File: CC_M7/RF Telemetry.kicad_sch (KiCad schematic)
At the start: 24 parts, among them U6 nRF52820-QDxx, U7 NRF21540-QDAA-R7, Y2 32MHz

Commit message: update
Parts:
- removed C43: 4.7uF, symbol Device:C_Small
- added J15: Conn_02x05_Odd_Even, symbol Connector_Generic:Conn_02x05_Odd_Even
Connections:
- net +3.3V: now also J15.10 (Pin_10)
- net GND: now also J15.2 (Pin_2), J15.6 (Pin_6), J15.8 (Pin_8)
- net RESET: now reaches U6.16 (P0.18/~{RESET})
- net RESET: now also J15.1 (Pin_1)
- net VBUS: no longer names the net of U6.10 (VBUS)
- new net SWCLCK: J15.7 (Pin_7)
- new net SWDIO: J15.9 (Pin_9)
- new net SWO: J15.5 (Pin_5)
- no-connect marks 0 -> 1
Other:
- note added: "Antenna"
- note added: "SWO Pins"
- note added: "VBUS hattı USB kullanılacağı zaman bağlanılacak."
- note added: "nRF OSC"
- note added: "nRF21540"
- note added: "nRF52820 and Decoupling"
- note removed: "VBUS hattı usb 5V hattı demektir"
- moved on the sheet: AE1, C31, C32, C33, C34, C35, C36, C37, C38, C39, C40, C41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

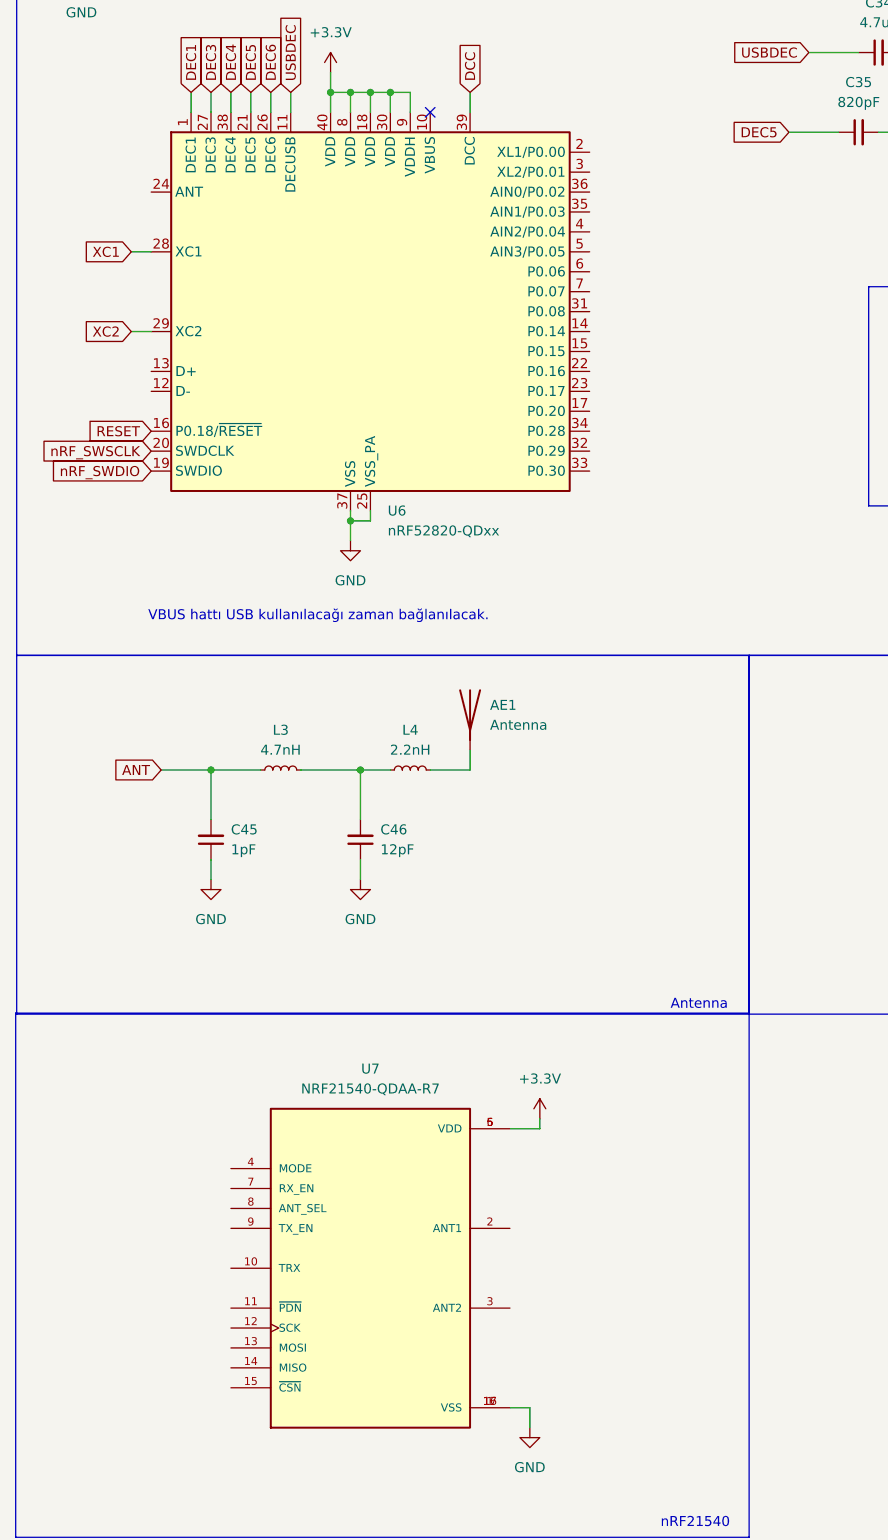
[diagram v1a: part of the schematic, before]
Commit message: NRF pins updated
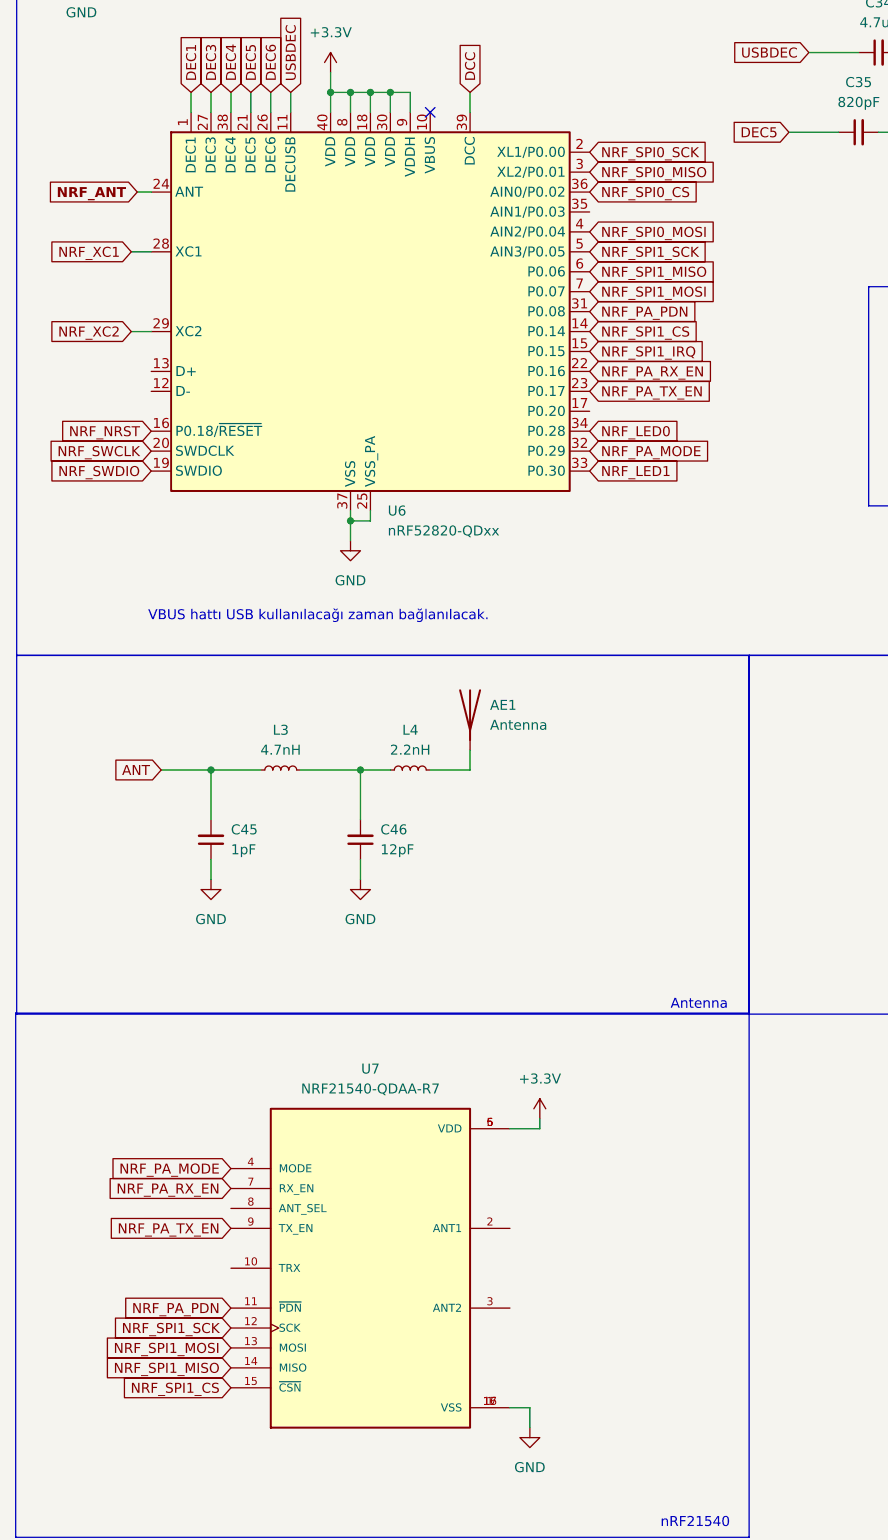
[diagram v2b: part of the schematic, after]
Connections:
- net RESET: no longer U6.16 (P0.18/~{RESET})
- net XC1: no longer U6.28 (XC1)
- net XC2: no longer U6.29 (XC2)
- net NRF_SPI1_CS: now reaches U6.14 (P0.14)
- net NRF_SPI1_CS: now also U7.15 (~{CSN})
- net NRF_SPI1_IRQ: now reaches U6.15 (P0.15)
- net NRF_SPI0_SCK: now reaches U6.2 (XL1/P0.00)
- net NRF_PA_RX_EN: now reaches U6.22 (P0.16)
- net NRF_PA_RX_EN: now also U7.7 (RX_EN)
- net NRF_PA_TX_EN: now reaches U6.23 (P0.17)
- net NRF_PA_TX_EN: now also U7.9 (TX_EN)
- net NRF_ANT: now reaches U6.24 (ANT)
- net NRF_SPI0_MISO: now reaches U6.3 (XL2/P0.01)
- net NRF_PA_PDN: now reaches U6.31 (P0.08)
- net NRF_PA_PDN: now also U7.11 (~{PDN})
- net NRF_PA_MODE : now reaches U6.32 (P0.29)
- net NRF_PA_MODE : now also U7.4 (MODE)
- net NRF_LED1: now reaches U6.33 (P0.30)
- net NRF_LED0: now reaches U6.34 (P0.28)
- net NRF_SPI0_CS: now reaches U6.36 (AIN0/P0.02)
- net NRF_SPI0_MOSI: now reaches U6.4 (AIN2/P0.04)
- net NRF_SPI1_SCK: now reaches U6.5 (AIN3/P0.05)
- net NRF_SPI1_SCK: now also U7.12 (SCK)
- net NRF_SPI1_MISO : now reaches U6.6 (P0.06)
- net NRF_SPI1_MISO : now also U7.14 (MISO)
- net NRF_SPI1_MOSI: now reaches U6.7 (P0.07)
- net NRF_SPI1_MOSI: now also U7.13 (MOSI)
- net nRF_SWDIO renamed NRF_SWDIO
- net nRF_SWSCLK renamed NRF_SWCLK
- new net NRF_NRST: U6.16 (P0.18/~{RESET})
- new net NRF_XC1: U6.28 (XC1)
- new net NRF_XC2: U6.29 (XC2)

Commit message: NRF
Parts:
- removed AE1: Antenna, symbol Device:Antenna
- removed C45: 1pF, symbol Device:C_Small
- removed C46: 12pF, symbol Device:C_Small
- removed L3: 4.7nH, symbol Device:L_Small
- removed L4: 2.2nH, symbol Device:L_Small
- added C28: 2pF, symbol Device:C_Small
- added C29: 1pF, symbol Device:C_Small
- added J9: Antenna, SMA_CONNECTOR:LPRS_SMA_CONNECTOR, symbol SMA_CONNECTOR:SMA_CONNECTOR
- added L6: 1.9nH, symbol Device:L_Small
- added L7: 3.0nH, symbol Device:L_Small
- added R15: 10k, symbol Device:R_Small
- added R16: 50R, symbol Device:R_Small
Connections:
- net GND: now also U7.8 (ANT_SEL), C28.2, C29.2, J9.G1, J9.G2, J9.G3, J9.G4, R16.2
- net NRF_ANT: now also U7.10 (TRX)
- net NRF_PA_MODE : now also R15.1; no longer U7.4 (MODE)
- net at U7.2 (ANT1): now also L6.1
- net at U7.3 (ANT2): now also R16.1
- new net: C28.1, L6.2, L7.1
- new net: C29.1, J9.1, L7.2
- new net: R15.2, U7.4 (MODE)
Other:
- note removed: "Antenna"
- note removed: "VBUS hattı USB kullanılacağı zaman bağlanılacak."
- moved on the sheet: C31, C32, C33, C34, C35, C36, C37, C44, J15, L1, L2, U7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

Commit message: nrf
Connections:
- net RESET is gone; now on net NRF_NRST: J15.1 (Pin_1)
- net SWCLCK is gone; now on net NRF_SWCLK: J15.7 (Pin_7)
- net SWDIO is gone; now on net NRF_SWDIO: J15.9 (Pin_9)
- net NRF_PA_MODE  renamed NRF_PA_MODE
- net NRF_SPI1_MISO  renamed NRF_SPI1_MISO
- net SWO: no longer names the net of J15.5 (Pin_5)
- no-connect marks 1 -> 4

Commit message: final schematic 6 warning
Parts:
- removed J15: Conn_02x05_Odd_Even, symbol Connector_Generic:Conn_02x05_Odd_Even
- added D5, D6: LED, symbol Device:LED
- added JP5, JP6, JP7, JP8: SWDIO, symbol Jumper:Jumper_2_Bridged
- added R17, R2: 1.5k, symbol Device:R_Small
- J9: value Antenna -> SMA_CONNECTOR
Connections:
- net XC1 is gone; now on net NRF_XC1: C32.2, Y2.1
- net XC2 is gone; now on net NRF_XC2: C44.2, Y2.3
- net GND: now also R17.1, R2.1
- net NRF_LED0: now also D5.2 (A)
- net NRF_LED1: now also D6.2 (A)
- net NRF_NRST: now also JP8.1 (A)
- net NRF_SPI0_CS: now also U7.15 (~{CSN})
- net NRF_SPI0_MISO: now also U7.14 (MISO)
- net NRF_SPI0_MOSI: now also U7.13 (MOSI)
- net NRF_SPI0_SCK: now also U7.12 (SCK)
- net NRF_SWCLK: now also JP6.1 (A)
- net NRF_SWDIO: now also JP7.1 (A)
- net +3.3V renamed 3V3_RF
- net 3V3_RF: now also JP5.1 (A)
- net NRF_SPI1_CS renamed SPI3_CS
- net SPI3_CS: no longer U7.15 (~{CSN})
- net NRF_SPI1_IRQ renamed SPI3_IRQ
- net NRF_SPI1_MISO renamed SPI3_MISO
- net SPI3_MISO: no longer U7.14 (MISO)
- net NRF_SPI1_MOSI renamed SPI3_MOSI
- net SPI3_MOSI: no longer U7.13 (MOSI)
- net NRF_SPI1_SCK renamed SPI3_SCK
- net SPI3_SCK: no longer U7.12 (SCK)
- new net: D6.1 (K), R17.2
- new net: D5.1 (K), R2.2
- new net J2_32: JP5.2 (B)
- new net J2_36: JP6.2 (B)
- new net J2_38: JP7.2 (B)
- new net J2_40: JP8.2 (B)
- no-connect marks 4 -> 5
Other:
- note added: "SWO"
- note added: "nRF52820"
- note removed: "SWO Pins"
- note removed: "nRF52820 and Decoupling"
- moved on the sheet: C28, C29, C31, C32, C33, C34, C35, C36, C37, C38, C39, C40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

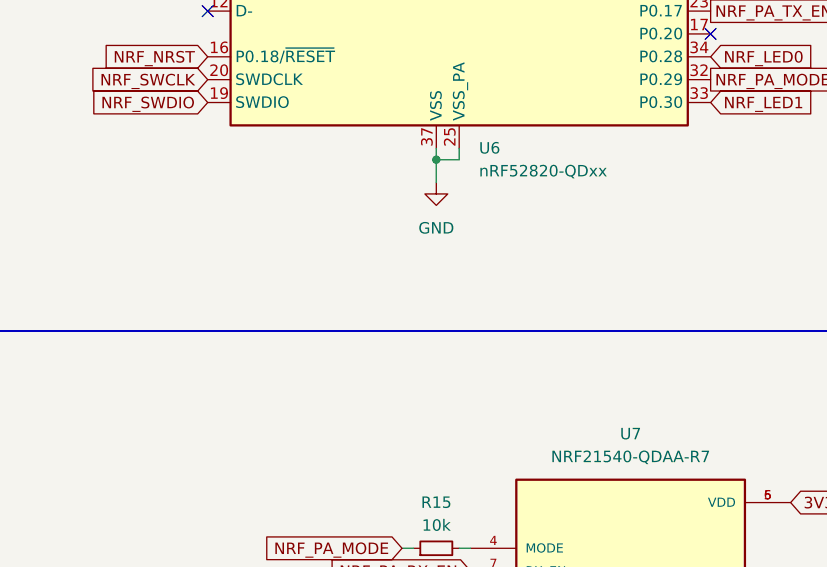
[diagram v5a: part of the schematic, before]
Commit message: schematic control comment
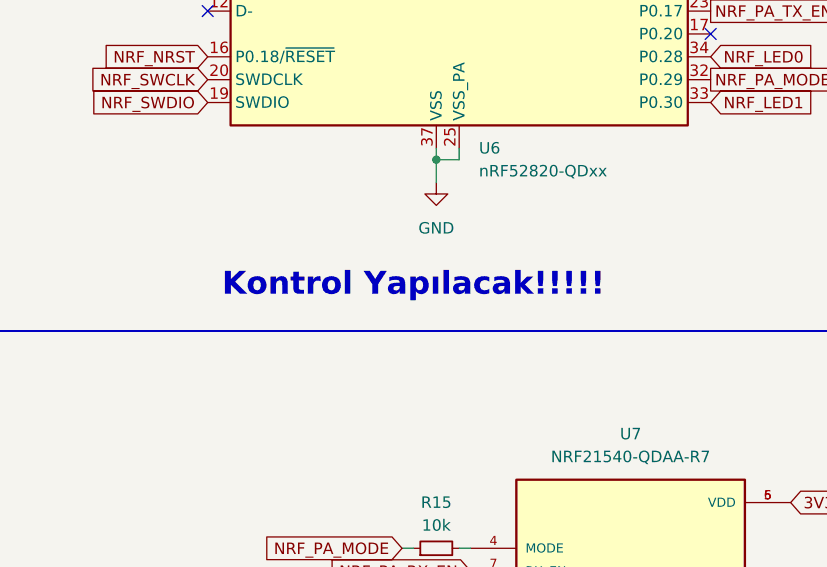
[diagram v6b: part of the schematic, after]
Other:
- note added: "Kontrol Yapılacak!!!!!"
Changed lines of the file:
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@@
+		)
+	)
+	(text "Kontrol Yapılacak!!!!!"
+		(exclude_from_sim no)
+		(at 69.85 139.7 0)
+		(effects
+			(font
+				(size 2.54 2.54)
+				(thickness 0.508)
+				(bold yes)
+			)
 		)
 	)

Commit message: Footprint assignment 1/2
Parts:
- C28, C29, C36, C39: footprint (none) -> Capacitor_SMD:C_0402_1005Metric
- C31, C32, C33, C35, C37, C38, C41, C42, C44: footprint (none) -> Capacitor_SMD:C_0201_0603Metric
- C34, C40: footprint (none) -> Capacitor_SMD:C_0603_1608Metric
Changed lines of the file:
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@@
 			)
 		)
-		(property "Footprint" ""
+		(property "Footprint" "Capacitor_SMD:C_0603_1608Metric"
 			(at 39.37 31.75 0)
 			(effects
@@
 			)
 		)
-		(property "Footprint" ""
+		(property "Footprint" "Capacitor_SMD:C_0201_0603Metric"
 			(at 69.85 31.75 0)
 			(effects
@@
 			)
 		)
-		(property "Footprint" ""
+		(property "Footprint" "Capacitor_SMD:C_0201_0603Metric"
 			(at 170.18 36.83 0)
 			(effects
@@
 			)
 		)
-		(property "Footprint" ""
+		(property "Footprint" "Capacitor_SMD:C_0402_1005Metric"
 			(at 170.18 26.67 0)
 			(effects
@@
 			)
 		)
-		(property "Footprint" ""
+		(property "Footprint" "Capacitor_SMD:C_0201_0603Metric"
 			(at 59.69 31.75 0)
 			(effects
@@
 			)
 		)
-		(property "Footprint" ""
+		(property "Footprint" "Capacitor_SMD:C_0402_1005Metric"
 			(at 30.48 31.75 0)
 			(effects
@@
 			)
 		)
-		(property "Footprint" ""
+		(property "Footprint" "Capacitor_SMD:C_0201_0603Metric"
 			(at 181.61 97.79 0)
 			(effects
@@
 			)
 		)
-		(property "Footprint" ""
+		(property "Footprint" "Capacitor_SMD:C_0402_1005Metric"
 			(at 142.24 181.61 0)
 			(effects
@@
 			)
 		)
-		(property "Footprint" ""
+		(property "Footprint" "Capacitor_SMD:C_0603_1608Metric"
 			(at 97.79 26.67 0)
 			(effects
@@
 			)
 		)
-		(property "Footprint" ""
+		(property "Footprint" "Capacitor_SMD:C_0201_0603Metric"
 			(at 49.53 31.75 0)
 			(effects
@@
 			)
 		)
-		(property "Footprint" ""
+		(property "Footprint" "Capacitor_SMD:C_0201_0603Metric"
 			(at 133.35 36.83 0)
 			(effects
@@
 			)
 		)
-		(property "Footprint" ""
+		(property "Footprint" "Capacitor_SMD:C_0402_1005Metric"
 			(at 127 181.61 0)
 			(effects
@@
 			)
 		)
-		(property "Footprint" ""
+		(property "Footprint" "Capacitor_SMD:C_0201_0603Metric"
 			(at 133.35 26.67 0)
 			(effects
@@
 			)
 		)
-		(property "Footprint" ""
+		(property "Footprint" "Capacitor_SMD:C_0201_0603Metric"
 			(at 162.56 97.79 0)
 			(effects
@@
 			)
 		)
-		(property "Footprint" ""
+		(property "Footprint" "Capacitor_SMD:C_0201_0603Metric"
 			(at 97.79 36.83 0)
 			(effects

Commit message: IIM42652 schematic added
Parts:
- C28, C29, C36, C39: footprint Capacitor_SMD:C_0402_1005Metric -> Capacitor_SMD:C_0603_1608Metric
- C31, C32, C33, C35, C37, C38, C41, C42: footprint Capacitor_SMD:C_0201_0603Metric -> Capacitor_SMD:C_0603_1608Metric
- D5, D6: footprint (none) -> LED_SMD:LED_0805_2012Metric
- L1, L2: footprint (none) -> Inductor_SMD:L_0603_1608Metric
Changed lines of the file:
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@@
 			)
 		)
-		(property "Footprint" "Capacitor_SMD:C_0201_0603Metric"
+		(property "Footprint" "Capacitor_SMD:C_0603_1608Metric"
 			(at 69.85 31.75 0)
 			(effects
@@
 			)
 		)
-		(property "Footprint" "Capacitor_SMD:C_0201_0603Metric"
+		(property "Footprint" "Capacitor_SMD:C_0603_1608Metric"
 			(at 170.18 36.83 0)
 			(effects
@@
 			)
 		)
-		(property "Footprint" "Capacitor_SMD:C_0402_1005Metric"
+		(property "Footprint" "Capacitor_SMD:C_0603_1608Metric"
 			(at 170.18 26.67 0)
 			(effects
@@
 			)
 		)
-		(property "Footprint" "Capacitor_SMD:C_0201_0603Metric"
+		(property "Footprint" "Capacitor_SMD:C_0603_1608Metric"
 			(at 59.69 31.75 0)
 			(effects
@@
 			)
 		)
-		(property "Footprint" ""
+		(property "Footprint" "LED_SMD:LED_0805_2012Metric"
 			(at 168.91 132.08 0)
 			(effects
@@
 			)
 		)
-		(property "Footprint" ""
+		(property "Footprint" "Inductor_SMD:L_0603_1608Metric"
 			(at 166.37 48.26 0)
 			(effects
@@
 			)
 		)
-		(property "Footprint" "Capacitor_SMD:C_0402_1005Metric"
+		(property "Footprint" "Capacitor_SMD:C_0603_1608Metric"
 			(at 30.48 31.75 0)
 			(effects
@@
 			)
 		)
-		(property "Footprint" ""
+		(property "Footprint" "LED_SMD:LED_0805_2012Metric"
 			(at 168.91 123.19 0)
 			(effects
@@
 			)
 		)
-		(property "Footprint" ""
+		(property "Footprint" "Inductor_SMD:L_0603_1608Metric"
 			(at 176.53 48.26 0)
 			(effects
@@
 			)
 		)
-		(property "Footprint" "Capacitor_SMD:C_0402_1005Metric"
+		(property "Footprint" "Capacitor_SMD:C_0603_1608Metric"
 			(at 142.24 181.61 0)
 			(effects
@@
 			)
 		)
-		(property "Footprint" "Capacitor_SMD:C_0201_0603Metric"
+		(property "Footprint" "Capacitor_SMD:C_0603_1608Metric"
 			(at 49.53 31.75 0)
 			(effects
@@
 			)
 		)
-		(property "Footprint" "Capacitor_SMD:C_0201_0603Metric"
+		(property "Footprint" "Capacitor_SMD:C_0603_1608Metric"
 			(at 133.35 36.83 0)
 			(effects
@@
 			)
 		)
-		(property "Footprint" "Capacitor_SMD:C_0402_1005Metric"
+		(property "Footprint" "Capacitor_SMD:C_0603_1608Metric"
 			(at 127 181.61 0)
 			(effects
@@
 			)
 		)
-		(property "Footprint" "Capacitor_SMD:C_0201_0603Metric"
+		(property "Footprint" "Capacitor_SMD:C_0603_1608Metric"
 			(at 133.35 26.67 0)
 			(effects
@@
 			)
 		)
-		(property "Footprint" "Capacitor_SMD:C_0201_0603Metric"
+		(property "Footprint" "Capacitor_SMD:C_0603_1608Metric"
 			(at 162.56 97.79 0)
 			(effects
@@
 			)
 		)
-		(property "Footprint" "Capacitor_SMD:C_0201_0603Metric"
+		(property "Footprint" "Capacitor_SMD:C_0603_1608Metric"
 			(at 97.79 36.83 0)
 			(effects
